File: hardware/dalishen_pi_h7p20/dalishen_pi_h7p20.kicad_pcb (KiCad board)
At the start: 4 copper layers, 92 x 64 mm, 248 parts, among them J10 RJ45_HR911130A, J1001 USB_C_Receptacle_USB2.0_16P, J2 USB_C_Receptacle_USB2.0_16P, J3 USB_A, J6 5V, J7 OV5640, J8 Conn_02x07_Odd_Even, J9 D500C930SV0, SW1 SW_Push, SW2 SW_Push, U1 YT8531C, U1001 AIC8800FC, U1002 P25Q80H/P25Q64H/P25Q128HA, U18 LM2903, U19 LM2903, U2 LM2903, U20 USB3343, U3 H7P20N0L128-M3H1, U4 SY7201ABC, U5 XC6206-2.8, U6 EA3036C, U7 P25Q32SH-SSH-IT, U8 XC6206-1.5, X2 XO32,26M, Y1 26M,NC, Y1001 26M, 10PPM, Y2 25M, 10PPM

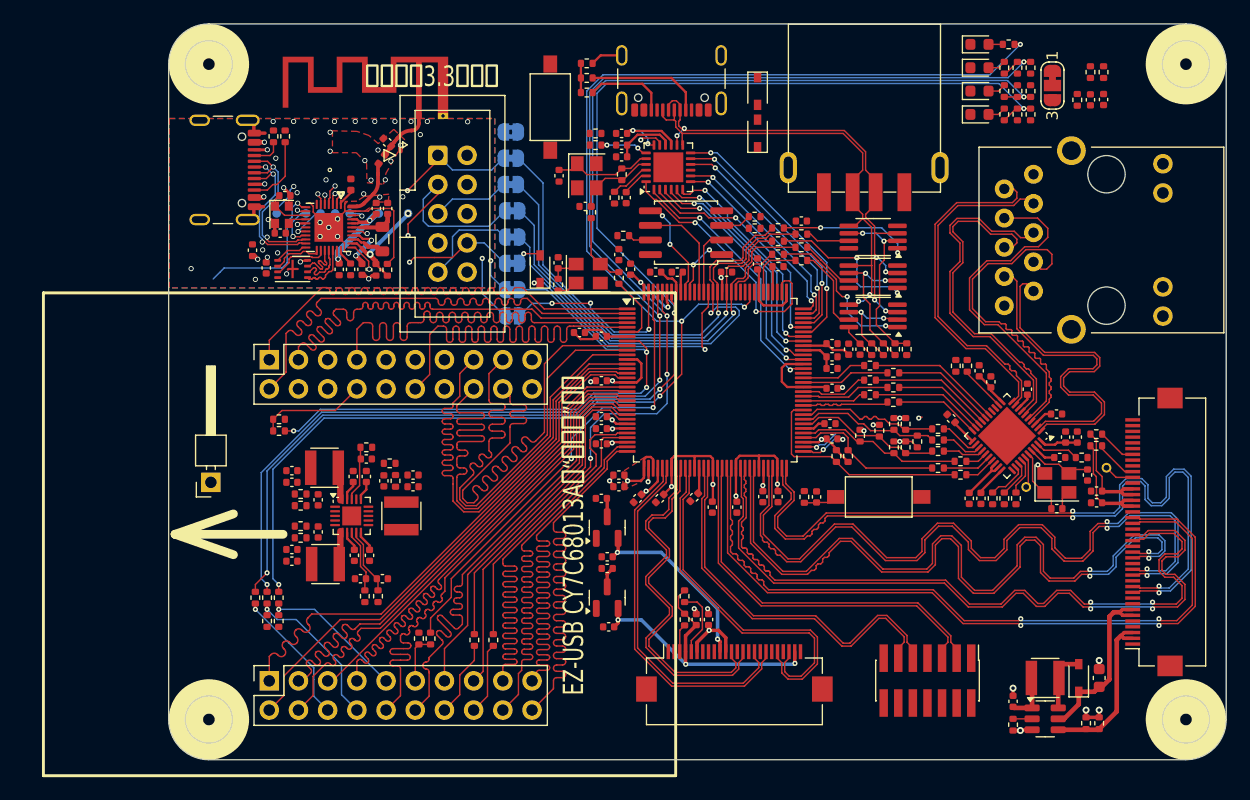
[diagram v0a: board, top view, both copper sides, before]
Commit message: [usb_sniffer_h7p20] 结构优化与验证
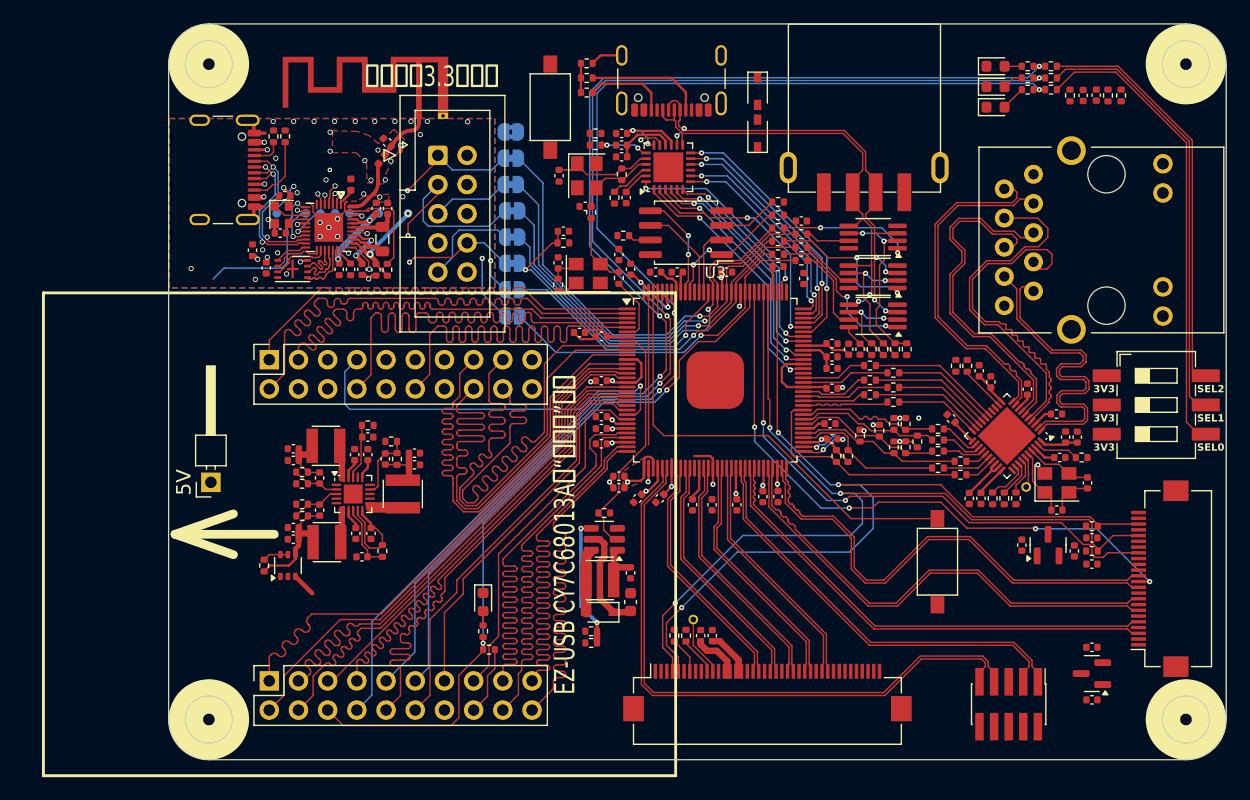
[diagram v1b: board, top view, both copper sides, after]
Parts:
- removed C41: 1uF,NC, Capacitor_SMD:C_0402_1005Metric
- removed D7: 1N5819(S4),NC, vllogic:D_SOD-323_BAT60
- removed J8: Conn_02x07_Odd_Even, Connector_PinHeader_1.27mm:PinHeader_2x07_P1.27mm_Vertical_SMD
- removed JP7, JP8: SolderJumper_2_Bridged, Jumper:SolderJumper-2_P1.3mm_Bridged_RoundedPad1.0x1.5mm
- removed R12, R13, R59, R60, R7: 5.1k, Resistor_SMD:R_0402_1005Metric
- removed R14, R17, R6, R67, R8, R9: 0,NC, Resistor_SMD:R_0402_1005Metric
- removed R37: 0, Resistor_SMD:R_0402_1005Metric
- removed R58: NC, Resistor_SMD:R_0402_1005Metric
- added J1: Conn_02x05_Odd_Even, Connector_PinHeader_1.27mm:PinHeader_2x05_P1.27mm_Vertical_SMD, F.Cu at (181.7, 148.8)
- added JP10: SolderJumper_2_Open, Jumper:SolderJumper-2_P1.3mm_Open_RoundedPad1.0x1.5mm, B.Cu at (138.5, 115.1)
- added SW3: SW_DIP_x03, Button_Switch_SMD:SW_DIP_SPSTx03_Slide_6.7x9.18mm_W8.61mm_P2.54mm_LowProfile, F.Cu at (194.6, 122.8)
- added U9: CJ3439KDW, Package_TO_SOT_SMD:SOT-363_SC-70-6, F.Cu at (119.0, 136.8)
- JP1: value SolderJumper_3_Bridged12 -> SolderJumper_2_Open; footprint Jumper:SolderJumper-3_P1.3mm_Bridged12_RoundedPad1.0x1.5mm_NumberLabels -> Jumper:SolderJumper-2_P1.3mm_Open_RoundedPad1.0x1.5mm; moved to B.Cu
- R16: value 0,NC -> 5.1k
- R35: value 5.1k -> 10k
- R36: value 10k -> 33k
- R5: value 5.1k -> 10k,1%
- R56, R57: value NC -> 5.1k
- U3: footprint Package_QFP:LQFP-128_14x14mm_P0.4mm -> vllogic:LQFP-128_14x14mm_P0.4mm_pad
- moved R19 68.5 mm to (136.0, 142.5), turned to -90 degrees
- moved D3 64.9 mm to (136.0, 140.0), turned to -90 degrees
- moved JP1 50.2 mm to (138.5, 112.8), turned to 180 degrees
- moved R65 44.9 mm to (145.4, 142.5), turned to 180 degrees
- moved C73 43.7 mm to (189.0, 148.5), turned to 180 degrees
- moved R64 43.6 mm to (145.4, 143.5), turned to 180 degrees
- moved U5 42.7 mm to (189.0, 146.2), turned to 180 degrees
- moved C72 42.1 mm to (189.0, 143.9)
- moved D8 42.0 mm to (146.2, 140.8), turned to 180 degrees
- moved U4 41.4 mm to (146.6, 134.5), turned to 180 degrees
- moved C69 41.3 mm to (148.8, 140.0)
- moved R22 40.7 mm to (152.7, 142.9), turned to 90 degrees
- moved C76 40.6 mm to (187.5, 135.5), turned to -90 degrees
- moved R63 40.0 mm to (146.6, 132.2), turned to 0 degrees
- moved L1 39.7 mm to (146.2, 138.0), turned to 180 degrees
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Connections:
- C44 pad 2: /VCCAUX -> /VDDIO_1V8
- C45 pad 2: /VCCAUX -> /VDDIO_1V8
- C54 pad 2: /VCCAUX -> /VDDIO_1V8
- C56 pad 2: /VCCAUX -> /VDDIO_1V8
- C70 pad 2: /VCCAUX -> /VDDIO_1V8
- C77 pad 2: /VCCAUX -> /VDDIO_1V8
- CY_J1 pad 7: /CY_SLWR -> /CY_SLRD
- CY_J1 pad 8: /CY_SLRD -> /CY_SLWR
- CY_J2 pad 11: /CY_SLOE -> /B1_IO_MSEL0_122
- CY_J2 pad 6: /CY_PA7 -> /B2_IO_CDONE_105
- CY_J2 pad 8: /CY_FIFOADDR1 -> /B1_IO_MSEL2_125
- CY_J2 pad 9: /CY_FIFOADDR0 -> /B1_IO_MSEL1_124
- J7 pad 10: /DVDD_1V5 -> GND
- J7 pad 11: /VCCAUX -> /B9_IO12N
- J7 pad 12: /B10_IO4P -> /OV_MCLK
- J7 pad 13: /OV_MCLK -> /B9_IO12P
- J7 pad 14: /B10_IO4N -> /VDDIO_1V8
- J7 pad 15: GND -> /DVDD_1V5
- J7 pad 16: /B10_IO2P -> unconnected-(J7-Pin_16-Pad16)
- J7 pad 17: unconnected-(J7-Pin_17-Pad17) -> /OV_PWDN
- J7 pad 18: /B10_IO2N -> unconnected-(J7-Pin_18-Pad18)
- J7 pad 19: unconnected-(J7-Pin_19-Pad19) -> /VDDIO_1V8
- J7 pad 2: GND -> /AVDD_2V8
- J7 pad 20: /B10_IO6P -> /OV/TP_SCL
- J7 pad 21: unconnected-(J7-Pin_21-Pad21) -> /AVDD_2V8
- J7 pad 22: /B10_IO6N -> /OV/TP_SDA
- J7 pad 23: /AVDD_2V8 -> GND
- J7 pad 3: /OV/TP_SDA -> /B9_IO6N
- J7 pad 4: /AVDD_2V8 -> unconnected-(J7-Pin_4-Pad4)
- J7 pad 5: /OV/TP_SCL -> /B9_IO6P
- J7 pad 6: /VCCAUX -> unconnected-(J7-Pin_6-Pad6)
- J7 pad 7: unconnected-(J7-Pin_7-Pad7) -> /B9_IO9N
- J7 pad 8: /OV_PWDN -> unconnected-(J7-Pin_8-Pad8)
- J7 pad 9: unconnected-(J7-Pin_9-Pad9) -> /B9_IO9P
- J9 pad 10: /B9_IO12P -> Net-(J9-Pin_10)
- J9 pad 11: /B9_IO12N -> Net-(J9-Pin_11)
- J9 pad 13: /B9_IO9P -> /VCC_3V3
- J9 pad 14: /B9_IO9N -> /VCC_3V3
- J9 pad 15: GND -> /VDDIO_1V8
- J9 pad 16: /B9_IO6P -> /VDDIO_1V8
- J9 pad 17: /B9_IO6N -> GND
- J9 pad 18: GND -> /B10_IO4N
- J9 pad 19: /B9_IO4P -> /B10_IO4P
- J9 pad 2: /LEDK -> /VCC_3V3
- J9 pad 20: /B9_IO4N -> GND
- J9 pad 21: GND -> /B10_IO6N
- J9 pad 22: /B9_IO2P -> /B10_IO6P
- J9 pad 23: /B9_IO2N -> GND
- J9 pad 24: GND -> /B10_IO9N
- J9 pad 25: /VCCAUX -> /B10_IO9P
- J9 pad 26: /VCCAUX -> GND
- J9 pad 27: /VCC_3V3 -> /B10_IO12N
- J9 pad 28: /VCC_3V3 -> /B10_IO12P
- J9 pad 3: /LEDK -> GND
- J9 pad 30: Net-(J9-Pin_30) -> /B9_IO2N
- J9 pad 31: Net-(J9-Pin_31) -> /B9_IO2P
- J9 pad 33: GND -> unconnected-(J9-Pin_33-Pad33)
- J9 pad 34: Net-(J9-Pin_34) -> /LEDA
- J9 pad 35: /TP_INT -> /LEDA
- J9 pad 36: /OV/TP_SDA -> unconnected-(J9-Pin_36-Pad36)
- J9 pad 37: /OV/TP_SCL -> unconnected-(J9-Pin_37-Pad37)
- J9 pad 38: GND -> /LEDK
- J9 pad 39: /VCC_3V3 -> /LEDK
- J9 pad 4: unconnected-(J9-Pin_4-Pad4) -> /OV/TP_SCL
- J9 pad 5: unconnected-(J9-Pin_5-Pad5) -> /OV/TP_SDA
- J9 pad 6: /LEDA -> /TP_INT
- J9 pad 7: /LEDA -> Net-(J9-Pin_7)
- J9 pad 8: unconnected-(J9-Pin_8-Pad8) -> GND
- JP1 pad 1: GND -> /FPGA_RX
- JP1 pad 2: /MSC -> /vllinkmodule/GPIOA7
- JP9 pad 1: Net-(D7-A) -> /CRST_N
- R16 pad 2: /B1_IO_MSEL1_124 -> /B2_IO_CDONE_105
- R21 pad 1: Net-(J9-Pin_31) -> Net-(J9-Pin_10)
- R21 pad 2: /VCCAUX -> /VDDIO_1V8
- R22 pad 1: Net-(J9-Pin_34) -> Net-(J9-Pin_7)
- R23 pad 2: /B3_IO_102 -> /FPGA_TX
- R24 pad 2: /OV_MCLK -> /FPGA_RX
- R5 pad 1: GND -> Net-(U9-D1)
- R5 pad 2: /CY_FIFOADDR0 -> /VCCAUX
- R55 pad 1: /B1_IO_MSEL0_122 -> Net-(R55-Pad1)
- R55 pad 2: /VCC_3V3 -> /B1_IO_MSEL0_122
- R56 pad 1: /B1_IO_MSEL1_124 -> Net-(R56-Pad1)
- R56 pad 2: /VCC_3V3 -> /B1_IO_MSEL1_124
- R57 pad 1: /B1_IO_MSEL2_125 -> Net-(R57-Pad1)
- R57 pad 2: /VCC_3V3 -> /B1_IO_MSEL2_125
- R63 pad 1: /B8_IO_126 -> /LED_PWM
- SW1 pad 1: /CRST_N -> /KEY
- TP1 pad 1: Net-(J9-Pin_30) -> Net-(J9-Pin_11)
- U3 pad 101: /OV_PWDN -> /OV/TP_SCL
- U3 pad 102: /B3_IO_102 -> /OV_PWDN
- U3 pad 104: /OV/TP_SDA -> /OV_MCLK
- U3 pad 106: /OV/TP_SCL -> /FPGA_TX
- U3 pad 107: /MSC -> GND
- U3 pad 108: /OV_MCLK -> /FPGA_RX
- U3 pad 126: /B8_IO_126 -> /KEY
- U3 pad 127: /B8_IO_127 -> /TP_INT
- U3 pad 24: /B7_IO_20 -> /CY_SLRD
- U3 pad 33: /VCCAUX -> /VDDIO_1V8
- U3 pad 35: /VCCAUX -> /VDDIO_1V8
- U3 pad 39: /VCCAUX -> /VDDIO_1V8
- U3 pad 48: /VCCAUX -> /VDDIO_1V8
- U3 pad 53: /VCCAUX -> /VDDIO_1V8
- U3 pad 62: /VCCAUX -> /VDDIO_1V8
- U3 pad 8: /B8_IO_8 -> /LED_PWM
- U3 pad 99: /TP_INT -> /OV/TP_SDA
- U4 pad 2: /B8_IO_126 -> /LED_PWM
- U6 pad 9: /ET3036C/EA3036_EN1 -> /VCC_5V
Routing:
- net /OV/TP_SDA: track 2.46 -> 79.3 mm, vias 0 -> 3
- net /OV/TP_SCL: track 6.00 -> 80.3 mm, vias 0 -> 3
- net /B2_IO_CDONE_105: track 126.8 -> 63.8 mm, vias 5 -> 2
- net /B8_IO_8: track 51.7 -> 0.00 mm, vias 3 -> 0
- net /OV_PWDN: track 0.00 -> 50.5 mm, vias 0 -> 2
- net /OV_MCLK: track 5.35 -> 53.8 mm, vias 0 -> 4
- net /B9_IO2P: track 63.7 -> 21.2 mm, vias 2 -> 0
- net /B9_IO2N: track 63.7 -> 21.2 mm, vias 2 -> 0
- net /B8_IO_126: track 42.0 -> 0.00 mm, vias 2 -> 0
- net Net-(R55-Pad1): track 0.00 -> 40.9 mm
- net /KEY: track 0.00 -> 39.7 mm
- net /vllinkmodule/5V: track 0.00 -> 39.2 mm, vias 0 -> 5
- net Net-(R56-Pad1): track 0.00 -> 38.3 mm
- net Net-(R57-Pad1): track 0.00 -> 35.8 mm
- net (no net): track 34.2 -> 0.00 mm
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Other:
- board text added: "3V3"
- board text added: "5V"
- board text added: "SEL0"
- board text added: "SEL1"
- board text added: "SEL2"

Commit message: [dalishen_pi_h7p20] backup
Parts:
- removed C2, C3: 0.1uF, Capacitor_SMD:C_0402_1005Metric
- removed D5, D6: 1N5819(S4), vllogic:D_SOD-323_BAT60
- removed R11: 0, Resistor_SMD:R_0402_1005Metric
- removed R4, R88: 33, Resistor_SMD:R_0402_1005Metric
- removed R66: NC, Resistor_SMD:R_0402_1005Metric
- removed X2: XO32,26M, vllogic:OSC_3225
- added C41: NC, Capacitor_SMD:C_0402_1005Metric, F.Cu at (97.7, 97.4)
- added C80: NC, Capacitor_SMD:C_0402_1005Metric, F.Cu at (97.7, 99.3)
- C12, C14: value 20pF,NC -> 9pF
- C4: value 10uF -> NC
- J2: footprint Connector_USB:USB_C_Receptacle_GCT_USB4105-xx-A_16P_TopMnt_Horizontal -> vllogic:USB_C_Receptacle_16P
- J3: footprint vllogic:USB-AF-180 -> vllogic:USB-AF_YIJIAN
- R1, R29, R30, R31, R32, R33, R34, R35, R44, R79, R90: value 10k -> 10k,1%
- R16, R23, R24, R25, R26, R27, R28, R55, R56, R57: value 5.1k -> 2.49k
- R45: value 2.49k,1% -> 2.49k
- R78: value 1M,NC -> 1M
- U18, U19, U2: value LM2903 -> LM2903A-VR
- Y1: value 26M,NC -> 26M
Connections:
- C1 pad 2: /VCC_3V3 -> /VCC_5V
- J2 pad S1: Net-(J2-SHIELD) -> GND
- J3 pad 5: Net-(J2-SHIELD) -> GND
- R90 pad 1: Net-(U20-ID) -> /VCC_3V3
- U18 pad 8: /VCC_3V3 -> /VCC_5V
- U19 pad 8: /VCC_3V3 -> /VCC_5V
- U2 pad 8: /VCC_3V3 -> /VCC_5V
- U3 pad 6: Net-(U3-IO13_PCLK_8) -> unconnected-(U3-IO13_PCLK_8-Pad6)
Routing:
- net /XO32_26M: track 6.23 -> 0.00 mm
- net Net-(U3-IO13_PCLK_8): track 5.78 -> 0.00 mm
- net Net-(J2-SHIELD): track 2.82 -> 0.00 mm
- net GND: track 34.3 -> 37.2 mm
- net /VCC_3V3: track 62.0 -> 59.3 mm
- net Net-(X2-EN): track 1.84 -> 0.00 mm

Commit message: [dalishen_pi_h7p20] backup
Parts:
- moved J3 0.77 mm to (169.2, 103.5)
- moved J1001 0.28 mm to (112.2, 102.4)
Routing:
- net /vllinkmodule/GPIOA5: track 13.8 -> 1.19 mm
- net /USB334x/USB20_D_N: track 44.0 -> 45.4 mm
- net /USB334x/USB20_D_P: track 40.5 -> 41.9 mm

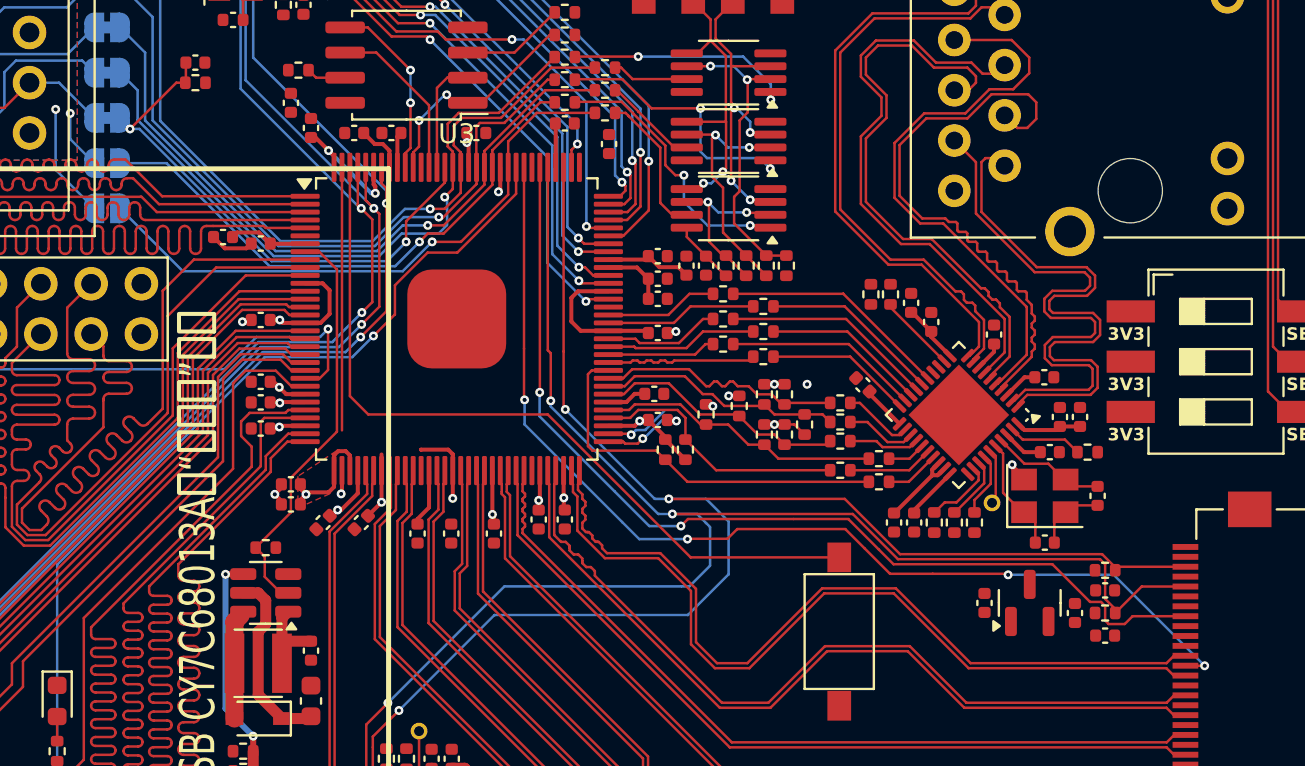
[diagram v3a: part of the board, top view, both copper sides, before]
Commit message: [usb_sniffer_h7p20] USB3343兼容CH132F，作相关调整
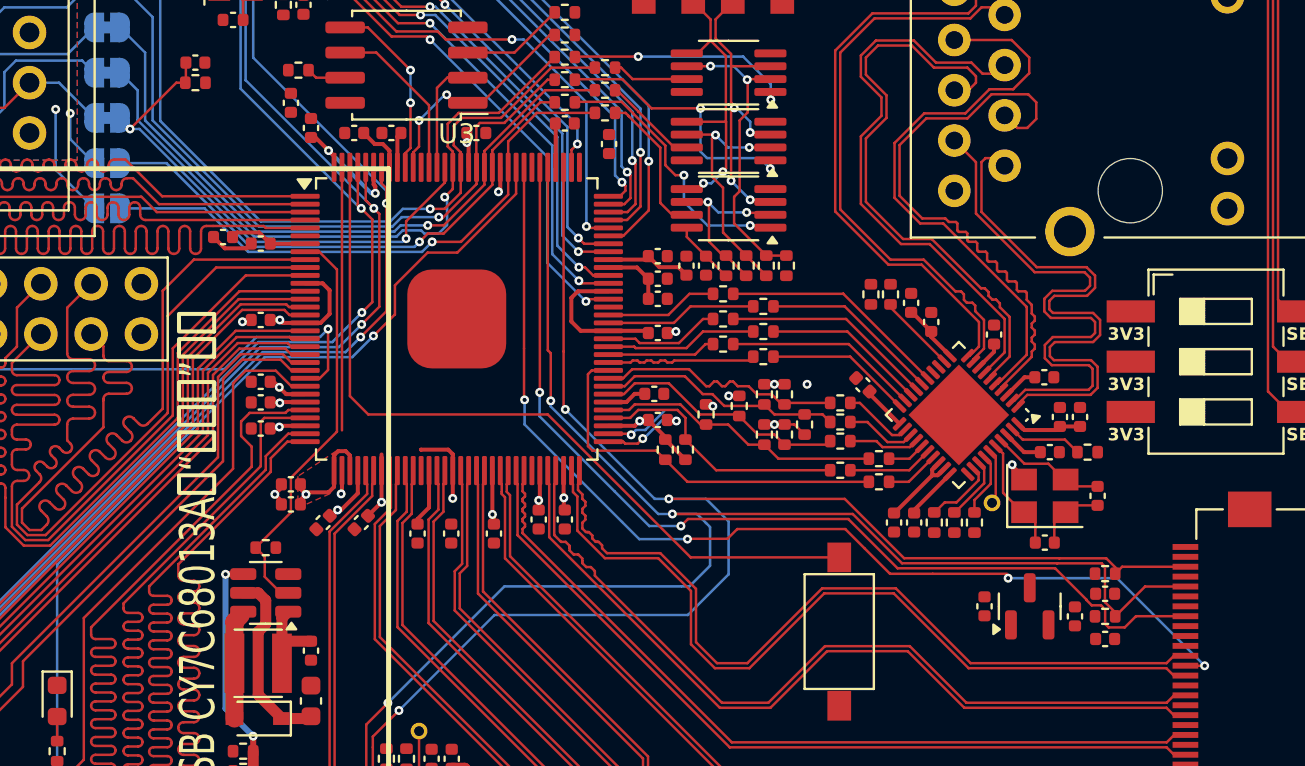
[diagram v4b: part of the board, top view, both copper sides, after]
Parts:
- moved C76 0.17 mm to (187.5, 135.7)
- moved C77 0.17 mm to (189.0, 136.8)
- moved R68 0.17 mm to (189.0, 135.7)
- moved C74 0.17 mm to (189.0, 134.5)
- moved C75 0.17 mm to (182.9, 135.2)
- moved R69 0.17 mm to (189.0, 133.5)
- moved U8 0.17 mm to (185.2, 135.2)
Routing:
- net /CRST_N: track 27.3 -> 26.4 mm
- net /FPGA_TDO: track 35.1 -> 34.2 mm
- net /FPGA_TMS: track 35.9 -> 35.1 mm
- net /FPGA_TCK: track 40.8 -> 40.0 mm
- net /FPGA_TX: track 30.2 -> 29.4 mm
- net /FPGA_RX: track 28.6 -> 27.8 mm
- net /FPGA_TDI: track 34.1 -> 33.5 mm
